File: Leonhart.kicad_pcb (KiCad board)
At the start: 2 copper layers, 3 parts, among them IC1 AM6231ASGGGAALW, IC2 CC2652P1FRGZR, U1 nRF52840

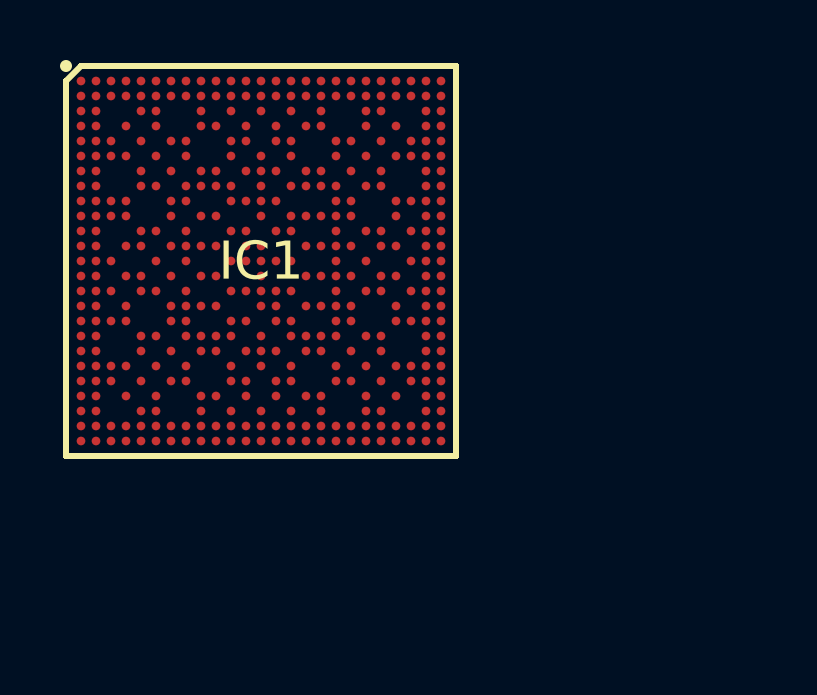
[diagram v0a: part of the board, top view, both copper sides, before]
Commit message: Started power circuitry and added more custom schematic symbols
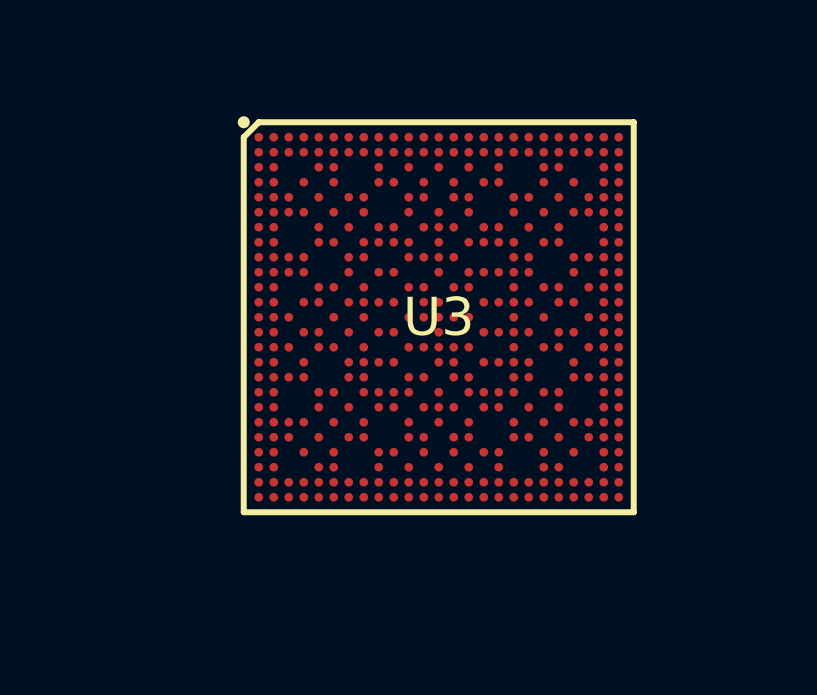
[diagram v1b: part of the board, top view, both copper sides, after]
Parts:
- removed IC1: AM6231ASGGGAALW, AM6231ASGGGAALW:BGA425C50P25X25_1300X1300X89
- added U3: AM6231ASGGGAALW, AM6231ASGGGAALW:BGA425C50P25X25_1300X1300X89, F.Cu at (158.7, 94.6)

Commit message: Small fixes
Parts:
- removed IC2: CC2652P1FRGZR, CC2652P1FRGZR:QFN50P700X700X100-49N-D
- removed U3: AM6231ASGGGAALW, AM6231ASGGGAALW:BGA425C50P25X25_1300X1300X89
- added U101: AM6231ASGGGAALW, AM6231ASGGGAALW:BGA425C50P25X25_1300X1300X89, F.Cu at (188.8, 92.7)
- added U703: TPD3S014, Package_TO_SOT_SMD:SOT-23-6, F.Cu at (149.7, 110.4)
- renumbered U1 to U301

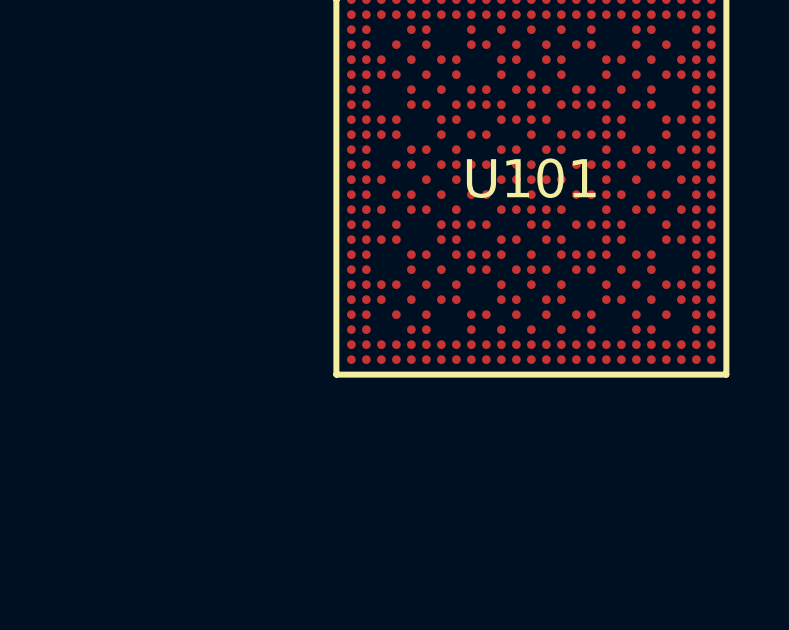
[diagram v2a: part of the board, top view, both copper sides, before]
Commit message: Almost finished Ethernet schematic
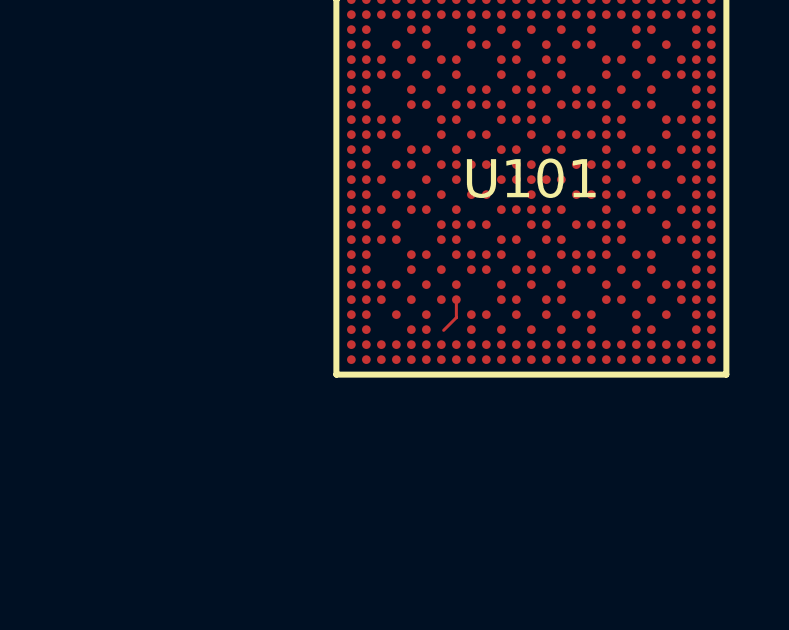
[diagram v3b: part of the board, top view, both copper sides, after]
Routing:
- net unconnected-(U101N-OLDI0_A2P-PadAA8): track 0.00 -> 1.20 mm
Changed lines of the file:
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@@
 		)
+	)
+	(segment
+		(start 186.25 97.25)
+		(end 185.825 97.675)
+		(width 0.1)
+		(layer "F.Cu")
+		(net 170)
+	)
+	(segment
+		(start 186.25 96.65)
+		(end 186.25 97.25)
+		(width 0.1)
+		(layer "F.Cu")
+		(net 170)
 	)
 	(embedded_fonts no)

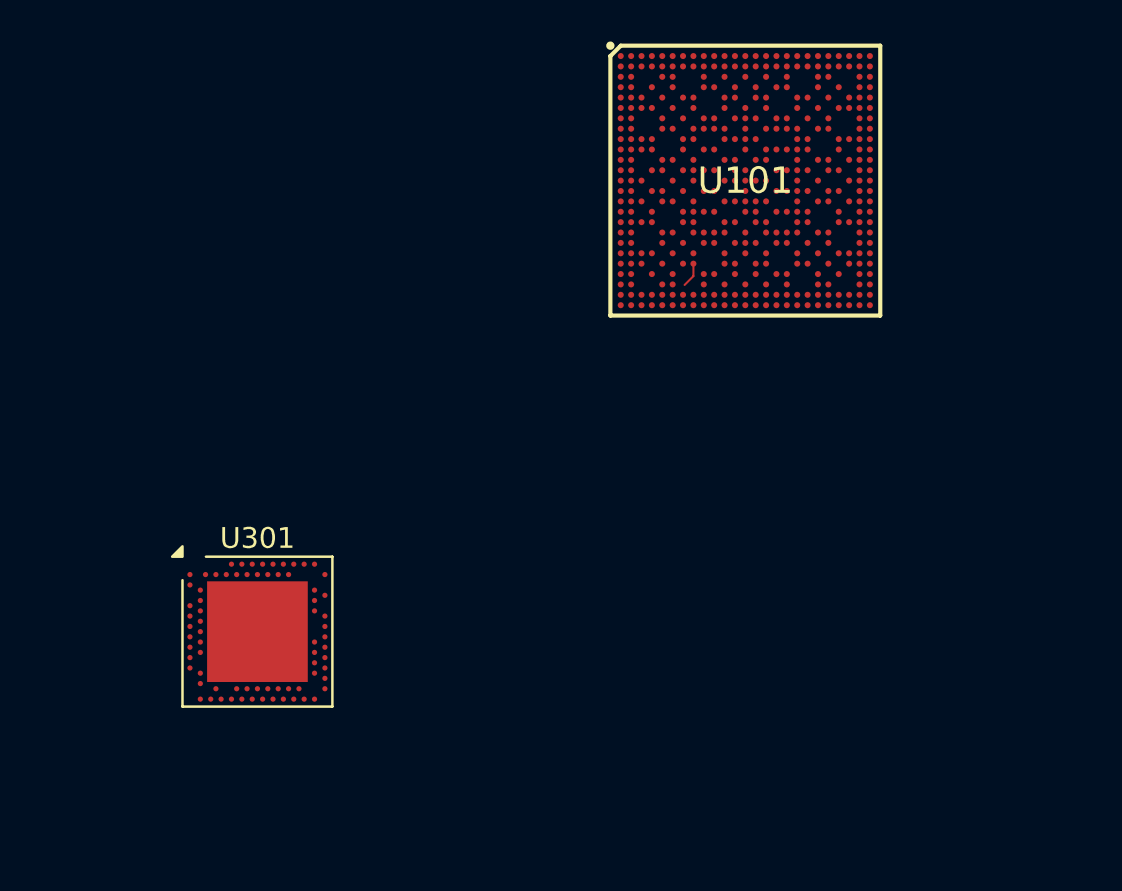
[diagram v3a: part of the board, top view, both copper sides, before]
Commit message: Fixed SoC power circuitry
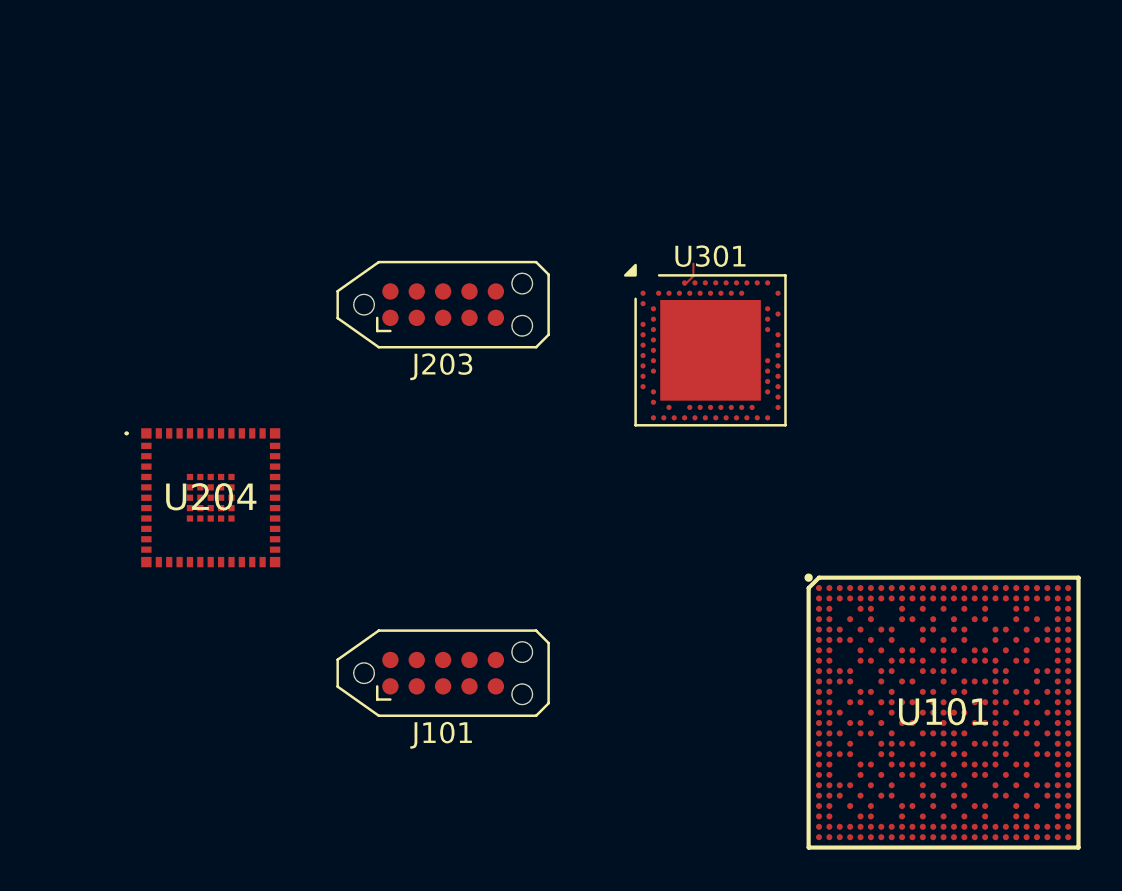
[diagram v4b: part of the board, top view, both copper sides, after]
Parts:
- added J101: TC2050, Connector:Tag-Connect_TC2050-IDC-NL_2x05_P1.27mm_Vertical, F.Cu at (174.2, 116.4)
- added J203: TC2050, Connector:Tag-Connect_TC2050-IDC-NL_2x05_P1.27mm_Vertical, F.Cu at (174.2, 98.6)
- added U204: CC2652PSIP, CC2652PSIP:CC2652PSIP, F.Cu at (163.0, 107.9)
- moved U101 27.3 mm to (198.3, 118.3)
- moved U301 25.7 mm to (187.1, 100.8)
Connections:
- net Net-(U301-VDD-PadA22) renamed VDD_nRF
- U101 pad A10: unconnected-(U101H-TCK-PadA10) -> /Host System [1]/SOC_TCK
- U101 pad A11: unconnected-(U101H-TDI-PadA11) -> /Host System [1]/SOC_TDI
- U101 pad A13: unconnected-(U101R-SPI0_CS0-PadA13) -> nRF_SPI0_CS0
- U101 pad A14: unconnected-(U101R-SPI0_CLK-PadA14) -> nRF_SPI0_CLK
- U101 pad A16: unconnected-(U101R-I2C0_SDA-PadA16) -> I2C0_SDA
- U101 pad A3: unconnected-(U101L-MCU_SPI0_OSC0_XO-PadA3) -> Net-(U101L-MCU_SPI0_OSC0_XO)
- U101 pad AA15: unconnected-(U101G-RGMII1_RD3-PadAA15) -> (no net)
- U101 pad AA18: unconnected-(U101G-RGMII2_TD1-PadAA18) -> (no net)
- U101 pad AA19: unconnected-(U101G-RGMII2_TX_CTL-PadAA19) -> (no net)
- U101 pad AA21: unconnected-(U101P-VOUT0_DATA15-PadAA21) -> GPIO0_60_eMMC_RSTn
- U101 pad AA23: unconnected-(U101P-VOUT0_DATA11-PadAA23) -> CC2652_UART6_CTSn
- U101 pad AB16: unconnected-(U101G-RGMII1_RD2-PadAB16) -> (no net)
- U101 pad AB17: unconnected-(U101G-RGMII1_RD0-PadAB17) -> (no net)
- U101 pad AB20: unconnected-(U101G-RGMII2_RD1-PadAB20) -> (no net)
- U101 pad AB22: unconnected-(U101J-MDIO0_MDIO-PadAB22) -> ETH_MDIO
- U101 pad AC17: unconnected-(U101G-RGMII1_RD1-PadAC17) -> (no net)
- U101 pad AC20: unconnected-(U101G-RGMII2_TD3-PadAC20) -> (no net)
- U101 pad AC21: unconnected-(U101G-RGMII2_RD2-PadAC21) -> (no net)
- U101 pad AD17: unconnected-(U101G-RGMII1_RXC-PadAD17) -> (no net)
- U101 pad AD18: unconnected-(U101G-RGMII1_TD3-PadAD18) -> (no net)
- U101 pad AD19: unconnected-(U101G-RGMII1_TX_CTL-PadAD19) -> (no net)
- U101 pad AD20: unconnected-(U101G-RGMII1_TD1-PadAD20) -> (no net)
- U101 pad AD21: unconnected-(U101G-RGMII2_TD2-PadAD21) -> (no net)
- U101 pad AD22: unconnected-(U101G-RGMII2_RX_CTL-PadAD22) -> (no net)
- U101 pad AD23: unconnected-(U101G-RGMII2_RXC-PadAD23) -> (no net)
- U101 pad AD24: unconnected-(U101J-MDIO0_MDC-PadAD24) -> ETH_MDC
- U101 pad AE17: unconnected-(U101G-RGMII1_RX_CTL-PadAE17) -> (no net)
- U101 pad AE18: unconnected-(U101G-RGMII1_TD2-PadAE18) -> (no net)
- U101 pad AE19: unconnected-(U101G-RGMII1_TXC-PadAE19) -> (no net)
- U101 pad AE20: unconnected-(U101G-RGMII1_TD0-PadAE20) -> (no net)
- U101 pad AE21: unconnected-(U101G-RGMII2_TXC-PadAE21) -> (no net)
- U101 pad AE22: unconnected-(U101G-RGMII2_RD3-PadAE22) -> (no net)
- U101 pad AE23: unconnected-(U101G-RGMII2_RD0-PadAE23) -> (no net)
- U101 pad B10: unconnected-(U101H-TRSTN-PadB10) -> /Host System [1]/SOC_TRST#
- U101 pad B11: unconnected-(U101H-TMS-PadB11) -> /Host System [1]/SOC_TMS
- U101 pad B12: unconnected-(U101Q-MCU_RESETSTATZ-PadB12) -> MCU_RESETSTATz
- U101 pad B13: unconnected-(U101R-SPI0_D0-PadB13) -> nRF_SPI0_MISO
- U101 pad B14: unconnected-(U101R-SPI0_D1-PadB14) -> nRF_SPI0_MOSI
- U101 pad B16: unconnected-(U101R-I2C0_SCL-PadB16) -> I2C0_SCL
- U101 pad B2: unconnected-(U101L-MCU_SPI0_OSC0_XI-PadB2) -> Net-(U101L-MCU_SPI0_OSC0_XI)
- U101 pad B7: unconnected-(U101J-PMIC_LPM_EN0-PadB7) -> PMIC_LPM_EN0
- U101 pad C1: unconnected-(U101J-WKUP_LFOSC0_XO-PadC1) -> /Host System [1]/WKUP_LFOSC0_XO
- U101 pad C11: unconnected-(U101H-EMU1-PadC11) -> /Host System [1]/SOC_EMU1
- U101 pad C2: unconnected-(U101J-WKUP_LFOSC0_XI-PadC2) -> /Host System [1]/WKUP_LFOSC0_XI
- U101 pad D1: unconnected-(U101Q-MCU_ERRORN-PadD1) -> MCU_SAFETY_ERRORz_1V8
- U101 pad D12: unconnected-(U101H-TDO-PadD12) -> /Host System [1]/SOC_TDO
- U101 pad D16: unconnected-(U101Q-EXTINTN-PadD16) -> EXTINTn
- U101 pad D2: unconnected-(U101Q-MCU_PORZ-PadD2) -> MCU_PORz
- U101 pad E11: unconnected-(U101Q-MCU_RESETZ-PadE11) -> MCU_RESETz
- U101 pad E12: unconnected-(U101H-EMU0-PadE12) -> /Host System [1]/SOC_EMU0
- U101 pad E21: unconnected-(U101Q-PORZ_OUT-PadE21) -> PORz_OUT
- U101 pad F20: unconnected-(U101Q-RESET_REQZ-PadF20) -> SoC_WARM_RESETz
- U101 pad F22: unconnected-(U101Q-RESETSTATZ-PadF22) -> RESETSTATz
- U101 pad J22: (no net) -> unconnected-(U101F-OSPI0_D7-PadJ22)
- U101 pad V20: unconnected-(U101P-VOUT0_DATA10-PadV20) -> CC2652_UART6_RTSn
- U101 pad V21: unconnected-(U101P-VOUT0_DATA8-PadV21) -> CC2652_UART6_RXD
- U101 pad W21: unconnected-(U101P-VOUT0_DATA9-PadW21) -> CC2652_UART6_TXD
- U101 pad Y18: unconnected-(U101G-RGMII2_TD0-PadY18) -> (no net)
- U101 pad Y22: unconnected-(U101P-VOUT0_DATA14-PadY22) -> GPIO0_59_ETH_RSTn
- U301 pad A23: unconnected-(U301-XC2-PadA23) -> Net-(U301-XC2)
- U301 pad AA24: unconnected-(U301-SWDCLK-PadAA24) -> /Thread [3]/nRF_SWDCLK
- U301 pad AB2: unconnected-(U301-DCCH-PadAB2) -> Net-(U301-DCCH)
- U301 pad AC24: unconnected-(U301-SWDIO-PadAC24) -> /Thread [3]/nRF_SWDIO
- U301 pad AC9: unconnected-(U301-P0.14-PadAC9) -> nRF_SPI0_MOSI
- U301 pad AD10: unconnected-(U301-P0.15-PadAD10) -> nRF_SPI0_MISO
- U301 pad AD8: unconnected-(U301-P0.13-PadAD8) -> nRF_SPI0_CLK
- U301 pad B24: unconnected-(U301-XC1-PadB24) -> Net-(U301-XC1)
- U301 pad B3: unconnected-(U301-DCC-PadB3) -> Net-(U301-DCC)
- U301 pad B5: unconnected-(U301-DEC4-PadB5) -> Net-(U301-DEC4)
- U301 pad B7: Net-(U301-VSS-PadB7) -> GND
- U301 pad C1: unconnected-(U301-DEC1-PadC1) -> Net-(U301-DEC1)
- U301 pad D2: unconnected-(U301-XL1/P0.00-PadD2) -> Net-(U301-XL1/P0.00)
- U301 pad D23: unconnected-(U301-DEC3-PadD23) -> Net-(U301-DEC3)
- U301 pad E24: unconnected-(U301-DEC6-PadE24) -> Net-(U301-DEC4)
- U301 pad EP: Net-(U301-VSS-PadB7) -> GND
- U301 pad F2: unconnected-(U301-XL2/P0.01-PadF2) -> Net-(U301-XL2/P0.01)
- U301 pad F23: unconnected-(U301-VSS_PA-PadF23) -> GND
- U301 pad H23: unconnected-(U301-ANT-PadH23) -> Net-(U301-ANT)
- U301 pad U1: unconnected-(U301-TRACEDATA1/P0.12-PadU1) -> nRF_SPI0_CS0
- U301 pad Y2: unconnected-(U301-VDDH-PadY2) -> VDD_HV
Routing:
- net unconnected-(U301-AIN7/P0.31-PadA8): track 0.00 -> 1.20 mm
- net unconnected-(U101N-OLDI0_A2P-PadAA8): track 1.20 -> 0.00 mm

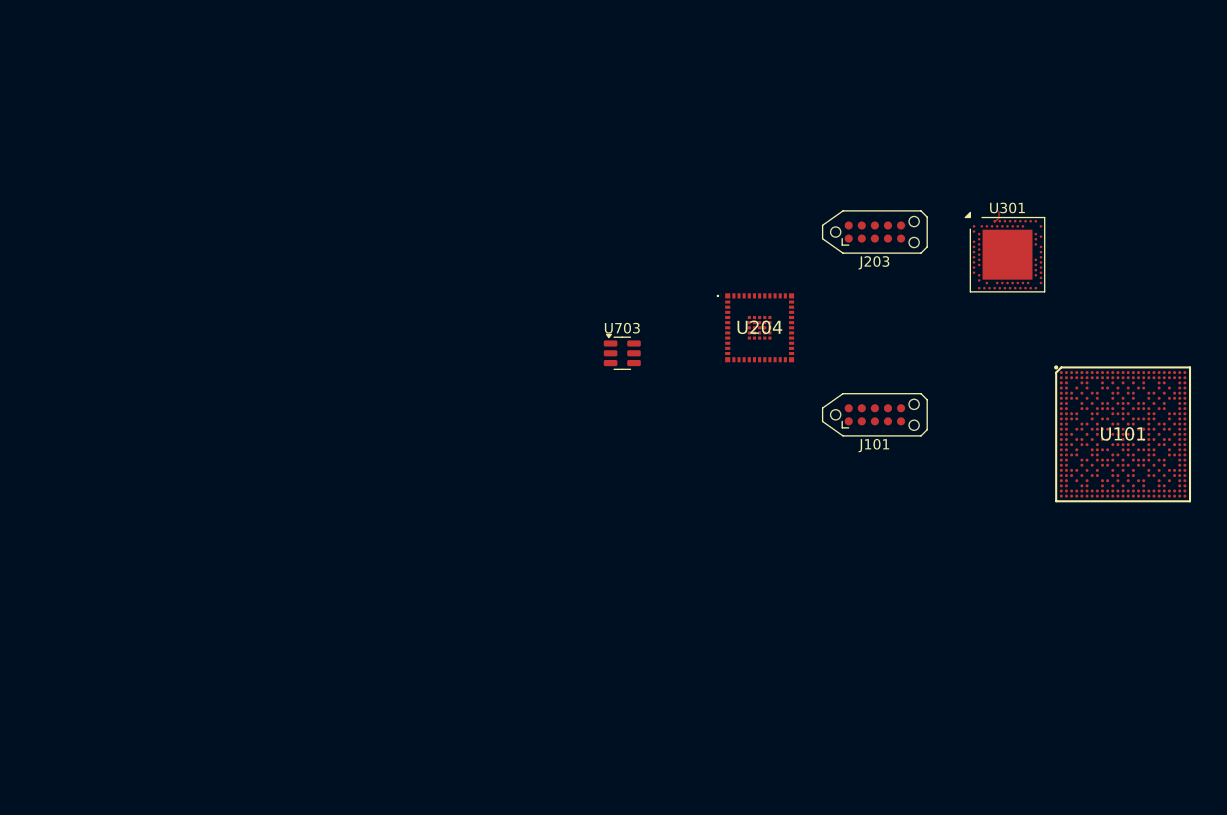
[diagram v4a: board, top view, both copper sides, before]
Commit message: Labeled all nets and added some footprints
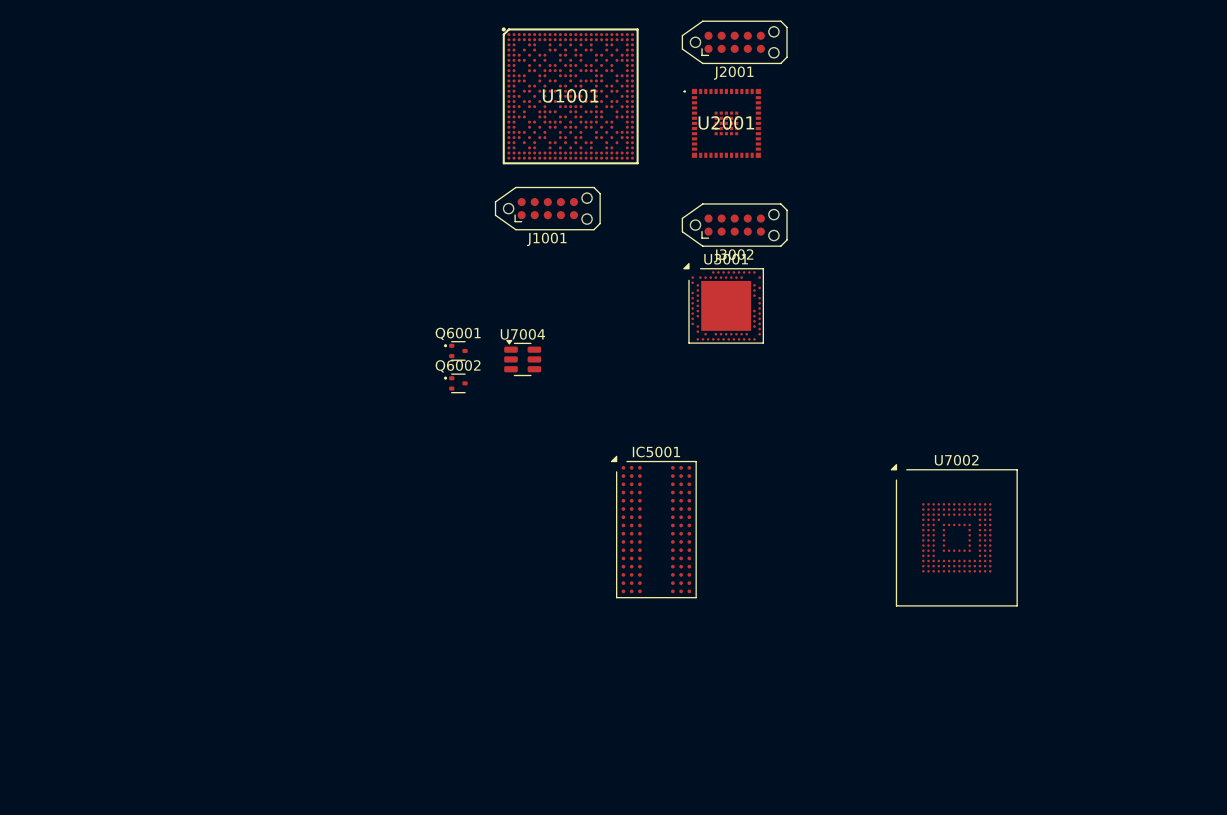
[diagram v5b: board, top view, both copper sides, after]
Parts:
- removed J101, J203: TC2050, Connector:Tag-Connect_TC2050-IDC-NL_2x05_P1.27mm_Vertical
- removed U101: AM6231ASGGGAALW, AM6231ASGGGAALW:BGA425C50P25X25_1300X1300X89
- removed U204: CC2652PSIP, CC2652PSIP:CC2652PSIP
- removed U301: nRF52840, Package_DFN_QFN:Nordic_AQFN-73-1EP_7x7mm_P0.5mm
- removed U703: TPD3S014, Package_TO_SOT_SMD:SOT-23-6
- added IC5001: MT40A1G16TB-062E_IT_F, Package_BGA:FBGA-96_7.5x13mm_Layout9x16_P0.8mm, F.Cu at (153.0, 127.5)
- added J1001: TC2050, Connector:Tag-Connect_TC2050-IDC-NL_2x05_P1.27mm_Vertical, F.Cu at (142.4, 96.3)
- added J2001: TC2050, Connector:Tag-Connect_TC2050-IDC-NL_2x05_P1.27mm_Vertical, F.Cu at (160.6, 80.2)
- added J3002: TC2050, Connector:Tag-Connect_TC2050-IDC-NL_2x05_P1.27mm_Vertical, F.Cu at (160.6, 98.0)
- added Q6001: DMG1012T, Package_TO_SOT_SMD:SOT-523, F.Cu at (133.7, 110.2)
- added Q6002: DMG1012T, Package_TO_SOT_SMD:SOT-523, F.Cu at (133.7, 113.3)
- added U1001: AM6231ASGGGAALW, AM6231ASGGGAALW:BGA425C50P25X25_1300X1300X89, F.Cu at (144.7, 85.5)
- added U2001: CC2652PSIP, CC2652PSIP:CC2652PSIP, F.Cu at (159.8, 88.1)
- added U3001: nRF52840, Package_DFN_QFN:Nordic_AQFN-73-1EP_7x7mm_P0.5mm, F.Cu at (159.8, 105.8)
- added U7002: EMMC16G-TB29-PZ90, Package_BGA:LFBGA-153_11.5x13mm_Layout14x14_P0.5mm, F.Cu at (182.2, 128.3)
- added U7004: TPD3S014, Package_TO_SOT_SMD:SOT-23-6, F.Cu at (140.0, 111.0)
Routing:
- net unconnected-(U301-AIN7/P0.31-PadA8): track 1.20 -> 0.00 mm
